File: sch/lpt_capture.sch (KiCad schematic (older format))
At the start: 2 parts, among them J1 DB25_Male_MountingHoles

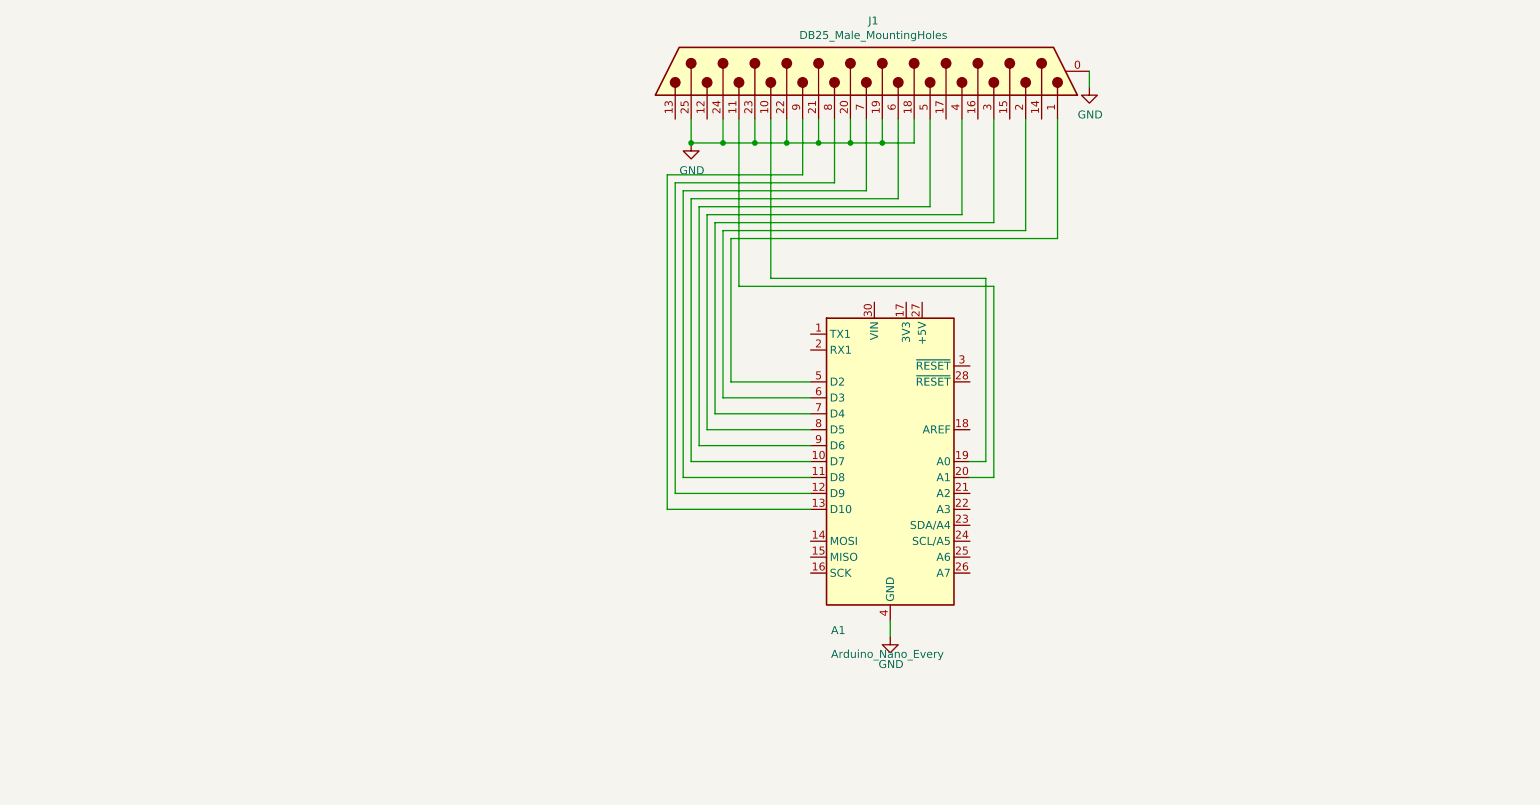
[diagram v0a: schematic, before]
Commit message: Add 1K resistors and a note to schematic.
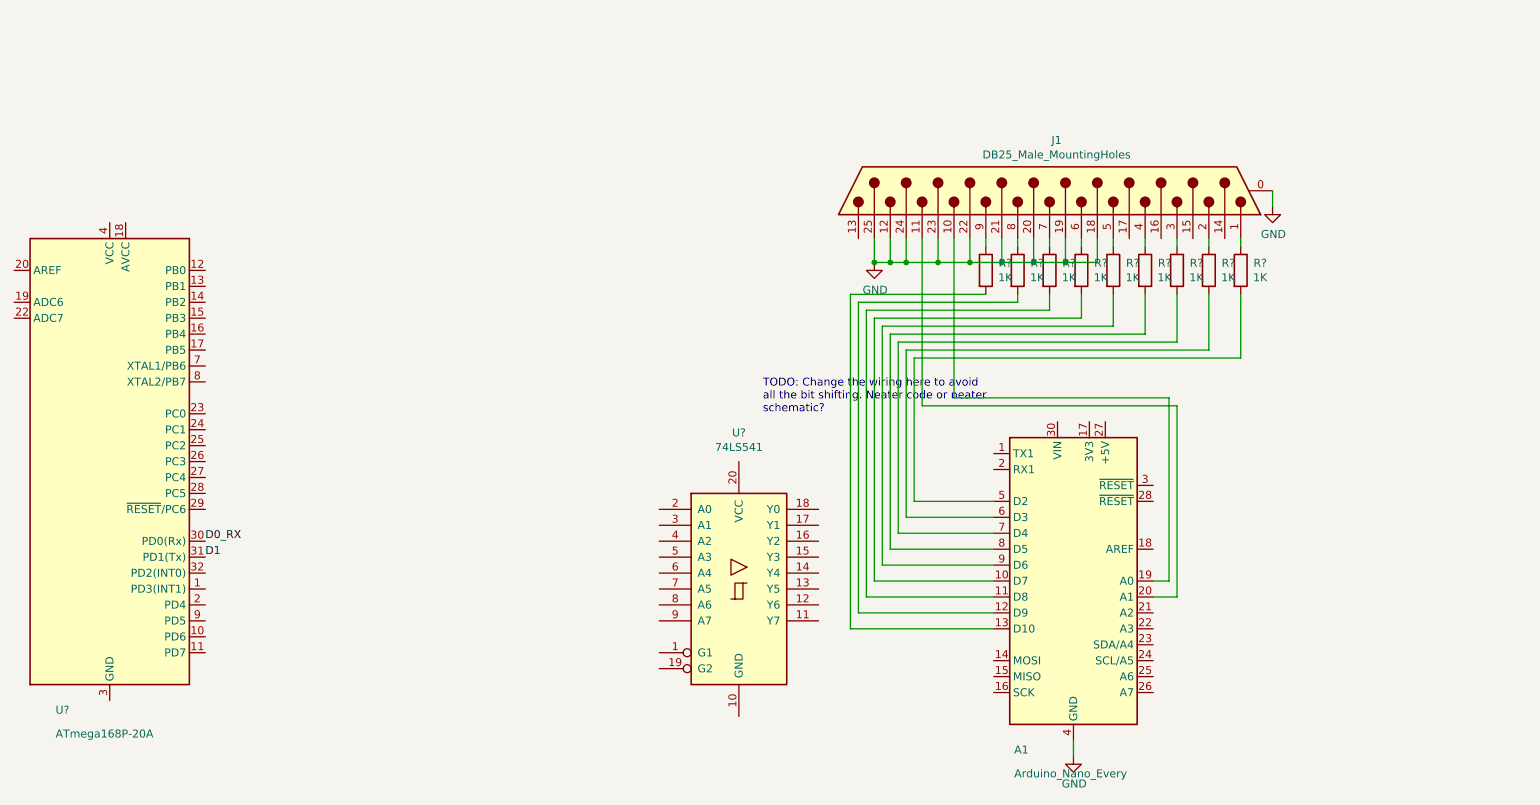
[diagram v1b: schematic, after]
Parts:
- added R? (x9): 1K, symbol Device:R
- added U?: 74LS541, symbol 74xx:74LS541
- added U?: ATmega168P-20A, Package_QFP:TQFP-32_7x7mm_P0.8mm, symbol MCU_Microchip_ATmega:ATmega168P-20A
- J1: footprint Connector_Dsub:DSUB-25_Male_Vertical_P2.77x2.84mm_MountingHoles -> Connector_Dsub:DSUB-25_Male_Horizontal_P2.77x2.84mm_EdgePinOffset4.94mm_Housed_MountingHolesOffset7.48mm
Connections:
- net GND: now also J1.12
- net at A1.10 (D7): now also R?.2; no longer J1.6
- net at A1.11 (D8): now also R?.2; no longer J1.7
- net at A1.12 (D9): now also R?.2; no longer J1.8
- net at A1.13 (D10): now also R?.2; no longer J1.9
- net at A1.5 (D2): now also R?.2; no longer J1.1
- net at A1.6 (D3): now also R?.2; no longer J1.2
- net at A1.7 (D4): now also R?.2; no longer J1.3
- net at A1.8 (D5): now also R?.2; no longer J1.4
- net at A1.9 (D6): now also R?.2; no longer J1.5
- new net: J1.1, R?.1
- new net: J1.2, R?.1
- new net: J1.3, R?.1
- new net: J1.4, R?.1
- new net: J1.5, R?.1
- new net: J1.6, R?.1
- new net: J1.7, R?.1
- new net: J1.8, R?.1
- new net: J1.9, R?.1
- new net: U?.21 (GND), U?.3 (GND), U?.5 (GND)
- new net: U?.4 (VCC), U?.6 (VCC)
- new net D0_RX: U?.30 (PD0(Rx))
- new net D1: U?.31 (PD1(Tx))
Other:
- note added: "TODO: Change the wiring here to avoid\nall the bit shifting. Neater code or neater\nschematic?"
- moved on the sheet: A1, J1

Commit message: Add REAL port names to schematic.
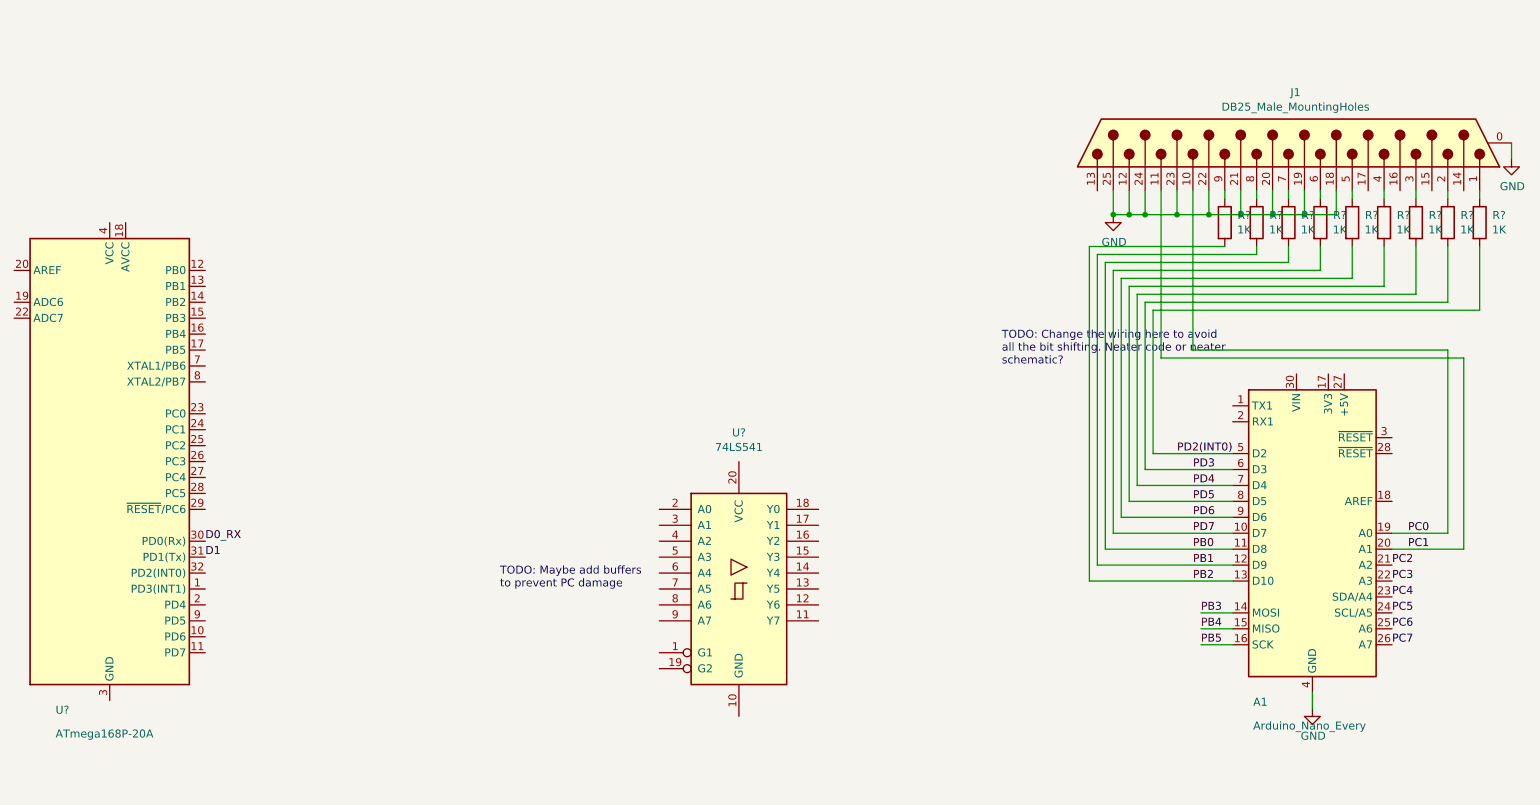
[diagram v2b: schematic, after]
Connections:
- net PD7: now reaches A1.10 (D7), R?.2
- net PB0: now reaches A1.11 (D8), R?.2
- net PB1: now reaches A1.12 (D9), R?.2
- net PB2: now reaches A1.13 (D10), R?.2
- net PB3: now reaches A1.14 (MOSI)
- net PB4: now reaches A1.15 (MISO)
- net PB5: now reaches A1.16 (SCK)
- net PC0: now reaches A1.19 (A0), J1.10
- net PC1: now reaches A1.20 (A1), J1.11
- net PC2: now reaches A1.21 (A2)
- net PC3: now reaches A1.22 (A3)
- net PC4: now reaches A1.23 (SDA/A4)
- net PC5: now reaches A1.24 (SCL/A5)
- net PC6: now reaches A1.25 (A6)
- net PC7: now reaches A1.26 (A7)
- net PD2(INT0): now reaches A1.5 (D2), R?.2
- net PD3: now reaches A1.6 (D3), R?.2
- net PD4: now reaches A1.7 (D4), R?.2
- net PD5: now reaches A1.8 (D5), R?.2
- net PD6: now reaches A1.9 (D6), R?.2
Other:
- note added: "TODO: Maybe add buffers \nto prevent PC damage"
- moved on the sheet: A1, J1, R?

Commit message: Do the PCB.
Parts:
- removed U?: ATmega168P-20A, Package_QFP:TQFP-32_7x7mm_P0.8mm, symbol MCU_Microchip_ATmega:ATmega168P-20A
- R1, R2, R3, R4, R5, R6, R7, R8, R9: renamed from R?; footprint (none) -> Resistor_THT:R_Axial_DIN0207_L6.3mm_D2.5mm_P7.62mm_Horizontal
- U2: renamed from U?; footprint (none) -> Package_DIP:DIP-20_W7.62mm_LongPads
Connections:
- no-connect marks 0 -> 8
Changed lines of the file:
@@
 	7400 1650 7400 1750
 $Comp
-L 74xx:74LS541 U?
+L 74xx:74LS541 U2
 U 1 1 5FE5F600
 P 2550 4450
-F 0 "U?" H 2550 5431 50  0000 C CNN
+F 0 "U2" H 2550 5431 50  0000 C CNN
 F 1 "74LS541" H 2550 5340 50  0000 C CNN
-F 2 "" H 2550 4450 50  0001 C CNN
+F 2 "Package_DIP:DIP-20_W7.62mm_LongPads" H 2550 4450 50  0001 C CNN
 F 3 "http://www.ti.com/lit/gpn/sn74LS541" H 2550 4450 50  0001 C CNN
 	1    2550 4450
@@
 $EndComp
 $Comp
-L Device:R R?
+L Device:R R9
 U 1 1 5FE5FFF9
 P 7200 2150
-F 0 "R?" H 7322 2196 50  0000 C CNN
+F 0 "R9" H 7322 2196 50  0000 C CNN
 F 1 "1K" H 7322 2105 50  0000 C CNN
-F 2 "" V 7130 2150 50  0001 C CNN
+F 2 "Resistor_THT:R_Axial_DIN0207_L6.3mm_D2.5mm_P7.62mm_Horizontal" V 7130 2150 50  0001 C CNN
 F 3 "~" H 7200 2150 50  0001 C CNN
 	1    7200 2150
@@
 	7200 2300 7200 2700
 $Comp
-L Device:R R?
+L Device:R R8
 U 1 1 5FE608AE
 P 7000 2150
-F 0 "R?" H 7122 2196 50  0000 C CNN
+F 0 "R8" H 7122 2196 50  0000 C CNN
 F 1 "1K" H 7122 2105 50  0000 C CNN
-F 2 "" V 6930 2150 50  0001 C CNN
+F 2 "Resistor_THT:R_Axial_DIN0207_L6.3mm_D2.5mm_P7.62mm_Horizontal" V 6930 2150 50  0001 C CNN
 F 3 "~" H 7000 2150 50  0001 C CNN
 	1    7000 2150
@@
 	7000 2300 7000 2650
 $Comp
-L Device:R R?
+L Device:R R7
 U 1 1 5FE60B0A
 P 6800 2150
-F 0 "R?" H 6922 2196 50  0000 C CNN
+F 0 "R7" H 6922 2196 50  0000 C CNN
 F 1 "1K" H 6922 2105 50  0000 C CNN
-F 2 "" V 6730 2150 50  0001 C CNN
+F 2 "Resistor_THT:R_Axial_DIN0207_L6.3mm_D2.5mm_P7.62mm_Horizontal" V 6730 2150 50  0001 C CNN
 F 3 "~" H 6800 2150 50  0001 C CNN
 	1    6800 2150
@@
 	6800 2300 6800 2600
 $Comp
-L Device:R R?
+L Device:R R6
 U 1 1 5FE60E1D
 P 6600 2150
-F 0 "R?" H 6722 2196 50  0000 C CNN
+F 0 "R6" H 6722 2196 50  0000 C CNN
 F 1 "1K" H 6722 2105 50  0000 C CNN
-F 2 "" V 6530 2150 50  0001 C CNN
+F 2 "Resistor_THT:R_Axial_DIN0207_L6.3mm_D2.5mm_P7.62mm_Horizontal" V 6530 2150 50  0001 C CNN
 F 3 "~" H 6600 2150 50  0001 C CNN
 	1    6600 2150
@@
 	6600 2300 6600 2550
 $Comp
-L Device:R R?
+L Device:R R5
 U 1 1 5FE60FC6
 P 6400 2150
-F 0 "R?" H 6522 2196 50  0000 C CNN
+F 0 "R5" H 6522 2196 50  0000 C CNN
 F 1 "1K" H 6522 2105 50  0000 C CNN
-F 2 "" V 6330 2150 50  0001 C CNN
+F 2 "Resistor_THT:R_Axial_DIN0207_L6.3mm_D2.5mm_P7.62mm_Horizontal" V 6330 2150 50  0001 C CNN
 F 3 "~" H 6400 2150 50  0001 C CNN
 	1    6400 2150
@@
 	6400 2300 6400 2500
 $Comp
-L Device:R R?
+L Device:R R4
 U 1 1 5FE61261
 P 6200 2150
-F 0 "R?" H 6322 2196 50  0000 C CNN
+F 0 "R4" H 6322 2196 50  0000 C CNN
 F 1 "1K" H 6322 2105 50  0000 C CNN
-F 2 "" V 6130 2150 50  0001 C CNN
+F 2 "Resistor_THT:R_Axial_DIN0207_L6.3mm_D2.5mm_P7.62mm_Horizontal" V 6130 2150 50  0001 C CNN
 F 3 "~" H 6200 2150 50  0001 C CNN
 	1    6200 2150
@@
 	6200 2300 6200 2450
 $Comp
-L Device:R R?
+L Device:R R3
 U 1 1 5FE61584
 P 6000 2150
-F 0 "R?" H 6122 2196 50  0000 C CNN
+F 0 "R3" H 6122 2196 50  0000 C CNN
 F 1 "1K" H 6122 2105 50  0000 C CNN
-F 2 "" V 5930 2150 50  0001 C CNN
+F 2 "Resistor_THT:R_Axial_DIN0207_L6.3mm_D2.5mm_P7.62mm_Horizontal" V 5930 2150 50  0001 C CNN
 F 3 "~" H 6000 2150 50  0001 C CNN
 	1    6000 2150
@@
 	6000 2300 6000 2400
 $Comp
-L Device:R R?
+L Device:R R2
 U 1 1 5FE617EF
 P 5800 2150
-F 0 "R?" H 5922 2196 50  0000 C CNN
+F 0 "R2" H 5922 2196 50  0000 C CNN
 F 1 "1K" H 5922 2105 50  0000 C CNN
-F 2 "" V 5730 2150 50  0001 C CNN
+F 2 "Resistor_THT:R_Axial_DIN0207_L6.3mm_D2.5mm_P7.62mm_Horizontal" V 5730 2150 50  0001 C CNN
 F 3 "~" H 5800 2150 50  0001 C CNN
 	1    5800 2150
@@
 	5800 2300 5800 2350
 $Comp
-L Device:R R?
+L Device:R R1
 U 1 1 5FE61A16
 P 5600 2150
-F 0 "R?" H 5722 2196 50  0000 C CNN
+F 0 "R1" H 5722 2196 50  0000 C CNN
 F 1 "1K" H 5722 2105 50  0000 C CNN
-F 2 "" V 5530 2150 50  0001 C CNN
+F 2 "Resistor_THT:R_Axial_DIN0207_L6.3mm_D2.5mm_P7.62mm_Horizontal" V 5530 2150 50  0001 C CNN
 F 3 "~" H 5600 2150 50  0001 C CNN
 	1    5600 2150
 	1    0    0    -1
 $EndComp
-$Comp
-L MCU_Microchip_ATmega:ATmega168P-20A U?
-U 1 1 5FE65C78
-P -1400 3650
-F 0 "U?" H -1740 2061 50  0000 L BNN
-F 1 "ATmega168P-20A" H -1740 1970 50  0000 L TNN
-F 2 "Package_QFP:TQFP-32_7x7mm_P0.8mm" H -1400 3650 50  0001 C CIN
-F 3 "http://ww1.microchip.com/downloads/en/DeviceDoc/Atmel-8025-8-bit-AVR-Microcontroller-ATmega48P-88P-168P_Datasheet.pdf" H -1400 3650 50  0001 C CNN
-	1    -1400 3650
-	1    0    0    -1
-$EndComp
-Text Label -800 4150 0    50   ~ 0
-D0_RX
-Text Label -800 4250 0    50   ~ 0
-D1
 Wire Wire Line
 	5000 1950 5000 2100
@@
 Text Notes 1050 4450 0    50   ~ 0
 TODO: Maybe add buffers \nto prevent PC damage
+NoConn ~ 7100 1950
+NoConn ~ 6900 1950
+NoConn ~ 6700 1950
+NoConn ~ 6500 1950
+NoConn ~ 4800 1950
+NoConn ~ 6650 3500
+NoConn ~ 6650 3600
+NoConn ~ 6650 3900
 $EndSCHEMATC

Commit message: Notes edit.
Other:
- note added: "TODO: Change the wiring here to avoid\nall the bit shifting. Neater code or neater\nPCB?"
- note removed: "TODO: Change the wiring here to avoid\nall the bit shifting. Neater code or neater\nschematic?"
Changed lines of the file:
@@
 encoding utf-8
 Sheet 1 1
-Title ""
-Date ""
-Rev ""
-Comp ""
+Title "LPT CAPTURE  BOARD"
+Date "2022-05-24"
+Rev "1"
+Comp "MILLSTREAM COMPUTING"
 Comment1 ""
 Comment2 ""
@@
 Wire Wire Line
 	5000 2100 5100 2100
-Text Notes 4200 3050 0    50   ~ 0
-TODO: Change the wiring here to avoid\nall the bit shifting. Neater code or neater\nschematic?
+Text Notes 5250 1150 0    50   ~ 0
+TODO: Change the wiring here to avoid\nall the bit shifting. Neater code or neater\nPCB?
 Text Label 5300 3600 0    50   ~ 0
 PD2(INT0)
